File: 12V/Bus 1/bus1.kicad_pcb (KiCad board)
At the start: 2 copper layers, 111.8 x 53 mm, 3 parts, among them J1 Conn_01x10_Pin

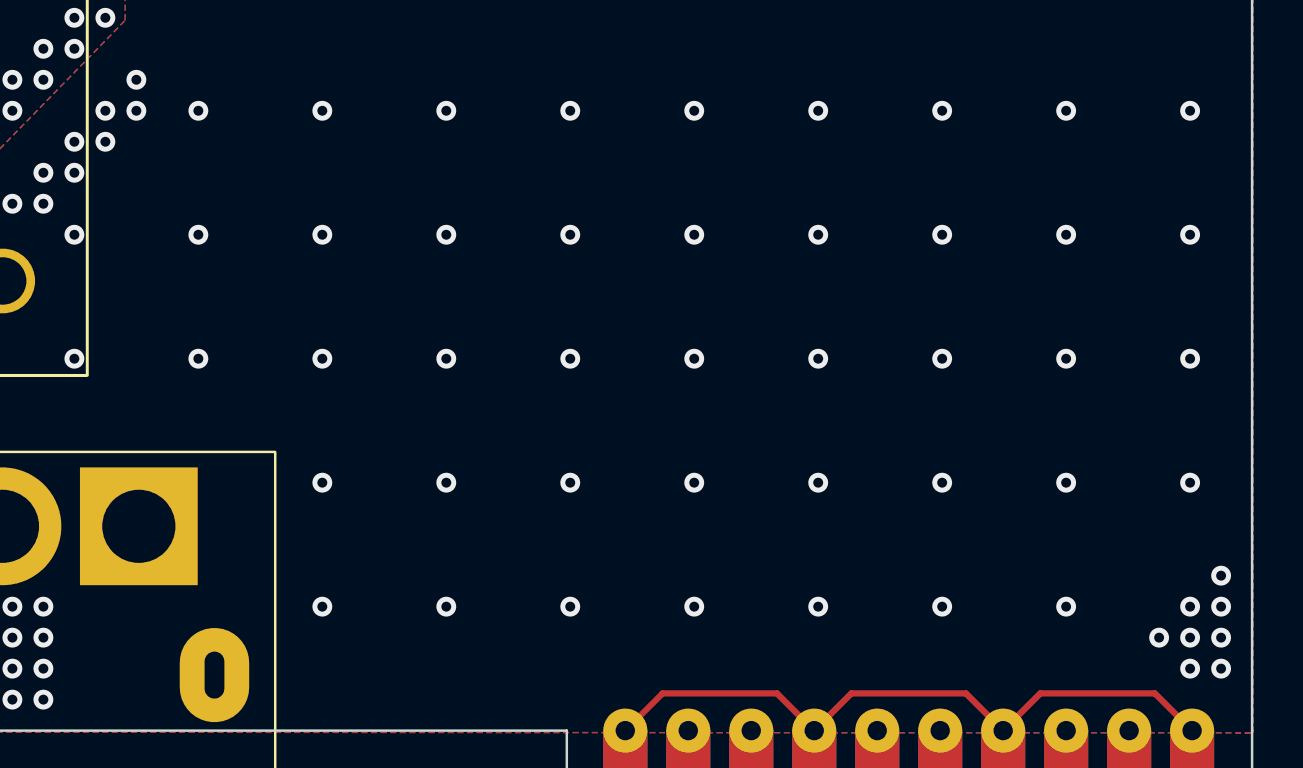
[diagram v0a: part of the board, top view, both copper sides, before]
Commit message: Bus silkscreens
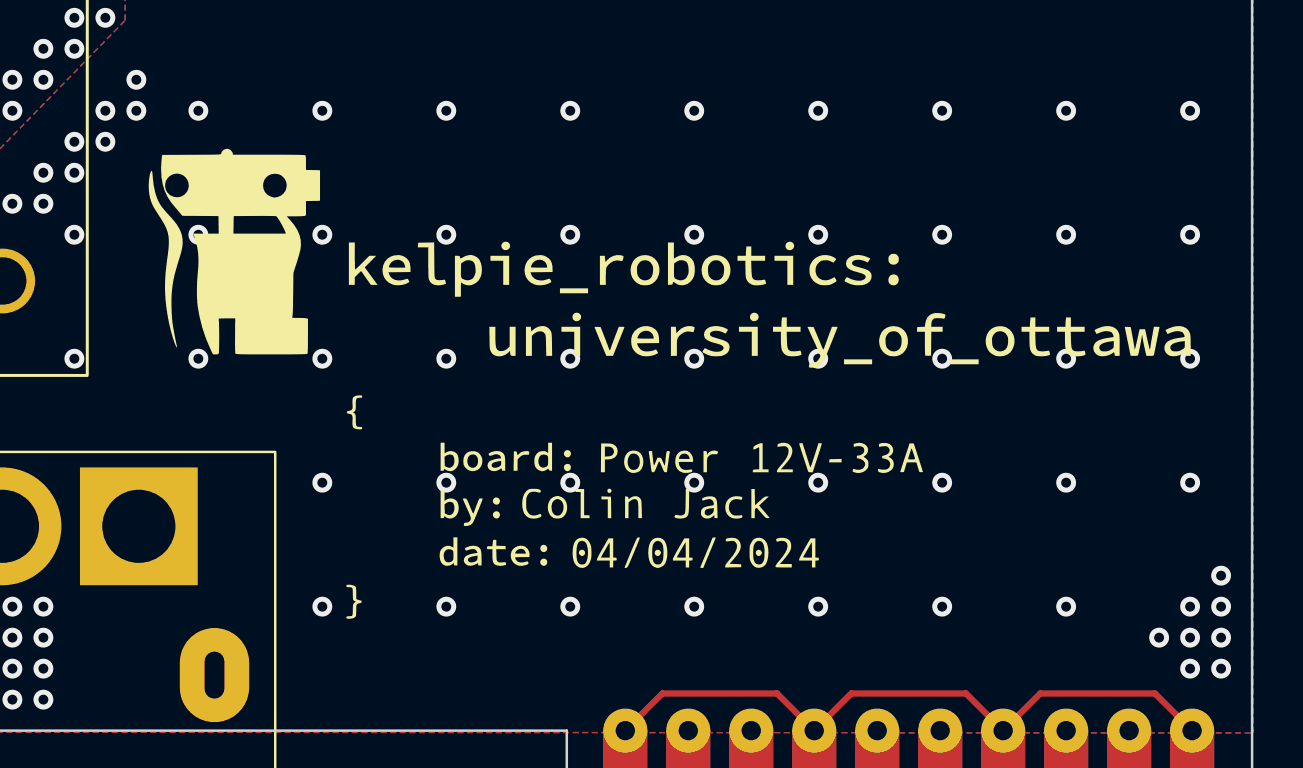
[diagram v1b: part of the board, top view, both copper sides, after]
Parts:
- added G***: LOGO, silks:12VBoard, F.Cu at (174.0, 86.0)
